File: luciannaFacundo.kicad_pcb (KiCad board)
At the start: 4 copper layers, 47 x 71.8 mm, 88 parts, among them J201 USB_B_Micro, J202 LiPo, J401 Conn_01x20, J402 Conn_01x20, Q201 MBT3904DW1, Q203 2.5A/30V, SW201 SW_DIP_x01, SW202 SW_DIP_x01, U201 MCP73831, U202 FT231XS, U203 AP2112K-3.3, U301 PCA9306, U302 ICM-20948, U401 ESP32, U402 W25Q32JVSS, Y401 26MHz, Y402 32.768kHz

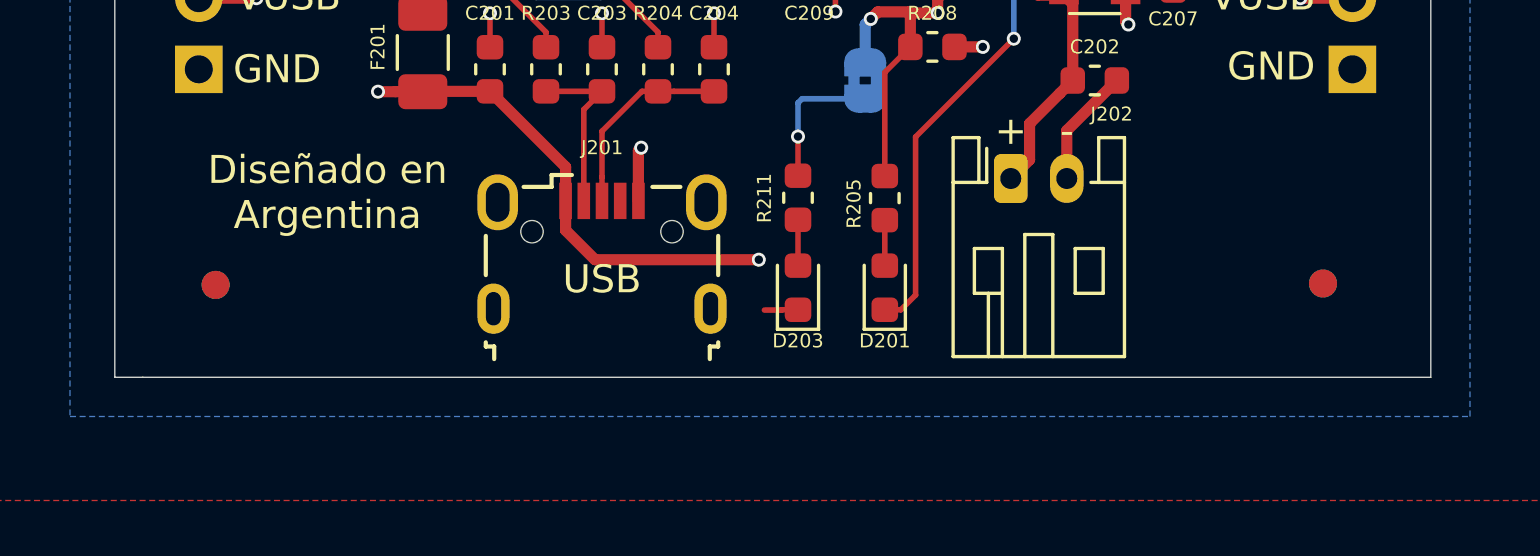
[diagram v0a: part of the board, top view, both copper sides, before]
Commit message: PMD03 - Creacion PCB y modelo 3D
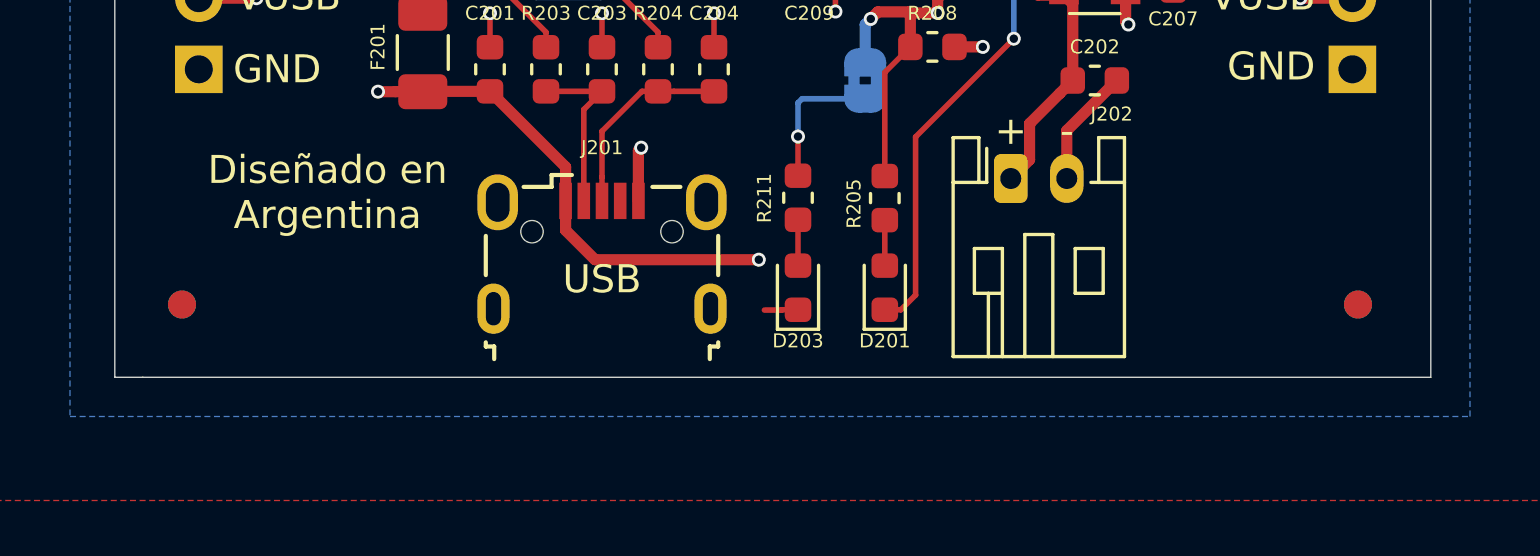
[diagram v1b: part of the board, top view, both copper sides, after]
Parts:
- moved REF03 1.46 mm to (142.0, 131.0)
- moved REF04 1.46 mm to (142.0, 131.0)
- moved REF02 1.39 mm to (100.0, 131.0)
- moved REF06 1.39 mm to (100.0, 131.0)
- moved REF** 1.34 mm to (106.0, 66.0)
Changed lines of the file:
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@@
   )
   (setup
-    (last_trace_width 0.2)
+    (last_trace_width 0.25)
     (user_trace_width 0.2)
     (user_trace_width 0.4)
@@
   )
   (module Fiducial:Fiducial_1mm_Mask3mm (layer B.Cu)
-    (at 101.2 130.3)
+    (at 100 131)
     (descr "Circular Fiducial, 1mm bare copper, 3mm soldermask opening (recommended)")
     (tags fiducial)
@@
   )
   (module Fiducial:Fiducial_1mm_Mask3mm (layer B.Cu)
-    (at 140.75 130.25)
+    (at 142 131)
     (descr "Circular Fiducial, 1mm bare copper, 3mm soldermask opening (recommended)")
     (tags fiducial)
@@
   )
   (module Fiducial:Fiducial_1mm_Mask3mm (layer F.Cu)
-    (at 140.75 130.25)
+    (at 142 131)
     (descr "Circular Fiducial, 1mm bare copper, 3mm soldermask opening (recommended)")
     (tags fiducial)
@@
   )
   (module Fiducial:Fiducial_1mm_Mask3mm (layer F.Cu)
-    (at 101.2 130.3)
+    (at 100 131)
     (descr "Circular Fiducial, 1mm bare copper, 3mm soldermask opening (recommended)")
     (tags fiducial)
@@
   )
   (module Symbol:OSHW-Symbol_6.7x6mm_SilkScreen (layer B.Cu)
-    (at 104.8 65.4 180)
+    (at 106 66 180)
     (descr "Open Source Hardware Symbol")
     (tags "Logo Symbol OSHW")
@@
     (effects (font (size 1 1) (thickness 0.15)))
   )
-  (via (at 115.6 107.8) (size 0.5) (drill 0.3) (layers F.Cu B.Cu) (net 10))
+  (segment (start 122.5875 74.45) (end 122.5875 72.9875) (width 0.75) (layer F.Cu) (net 1))
+  (segment (start 121.9 72.3) (end 121.9 71.3) (width 0.75) (layer F.Cu) (net 1))
+  (segment (start 122.5875 72.9875) (end 121.9 72.3) (width 0.75) (layer F.Cu) (net 1))
+  (segment (start 122.5875 75.45) (end 123.3 76.1625) (width 0.75) (layer F.Cu) (net 1))
+  (segment (start 122.5875 74.45) (end 122.5875 75.45) (width 0.75) (layer F.Cu) (net 1))
   (via (at 122.8 90.8) (size 0.5) (drill 0.3) (layers F.Cu B.Cu) (net 2))
   (via (at 121.2 90.8) (size 0.5) (drill 0.3) (layers F.Cu B.Cu) (net 2))
@@
   (via (at 121.2 88) (size 0.5) (drill 0.3) (layers F.Cu B.Cu) (net 2))
   (via (at 119.6 88) (size 0.5) (drill 0.3) (layers F.Cu B.Cu) (net 2))
-  (segment (start 122.5875 74.45) (end 122.5875 72.9875) (width 0.75) (layer F.Cu) (net 1))
-  (segment (start 121.9 72.3) (end 121.9 71.3) (width 0.75) (layer F.Cu) (net 1))
-  (segment (start 122.5875 72.9875) (end 121.9 72.3) (width 0.75) (layer F.Cu) (net 1))
-  (segment (start 122.5875 75.45) (end 123.3 76.1625) (width 0.75) (layer F.Cu) (net 1))
-  (segment (start 122.5875 74.45) (end 122.5875 75.45) (width 0.75) (layer F.Cu) (net 1))
   (segment (start 109.4 70.4) (end 109.625 70.625) (width 0.75) (layer In1.Cu) (net 2))
   (segment (start 130.4 79.55) (end 130.4 78.2) (width 0.2) (layer F.Cu) (net 2))
@@
   (segment (start 109.5875 98.2) (end 109.5875 99.7125) (width 0.2) (layer F.Cu) (net 9))
   (segment (start 109.45 99.85) (end 109.95 99.85) (width 0.2) (layer F.Cu) (net 9))
+  (via (at 115.6 107.8) (size 0.5) (drill 0.3) (layers F.Cu B.Cu) (net 10))
   (segment (start 118.8 97.9) (end 118.8 96.2) (width 0.2) (layer B.Cu) (net 10))
   (segment (start 118.8 96.2) (end 118.8 96.2) (width 0.2) (layer B.Cu) (net 10))

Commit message: Correcciones
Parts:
- removed REF** (x4): Fiducial_0.5mm_Mask1mm, Fiducial:Fiducial_0.5mm_Mask1mm
- removed REF**: OSHW-Symbol_6.7x6mm_SilkScreen, Symbol:OSHW-Symbol_6.7x6mm_SilkScreen
- removed REF**: KiCad-Logo2_5mm_SilkScreen, Symbol:KiCad-Logo2_5mm_SilkScreen
- removed REF01: Fiducial_1mm_Mask3m, Fiducial:Fiducial_1mm_Mask3mm
- removed REF02, REF03, REF04, REF05, REF06: Fiducial_1mm_Mask3mm, Fiducial:Fiducial_1mm_Mask3mm
- added FID101: Fiducial, Fiducial:Fiducial_1mm_Mask3mm, F.Cu at (142.0, 131.0)
- added FID102: Fiducial, Fiducial:Fiducial_1mm_Mask3mm, B.Cu at (100.0, 131.0)
- added FID103: Fiducial, Fiducial:Fiducial_1mm_Mask3mm, F.Cu at (100.0, 64.0)
- added FID104: Fiducial, Fiducial:Fiducial_1mm_Mask3mm, B.Cu at (142.0, 131.0)
- added FID105: Fiducial, Fiducial:Fiducial_1mm_Mask3mm, F.Cu at (100.0, 131.0)
- added FID106: Fiducial, Fiducial:Fiducial_1mm_Mask3mm, B.Cu at (100.0, 64.0)
- added LOGO101: Logo_Open_Hardware, Symbol:OSHW-Logo2_7.3x6mm_SilkScreen, B.Cu at (106.0, 66.0)
- added LOGO102: Logo_Kicad, Symbol:KiCad-Logo2_5mm_SilkScreen, B.Cu at (135.8, 66.0)
- J201: footprint Connector_USB:USB_Micro-B_Wuerth_629105150521 -> Connector_USB:USB_Micro-B_GCT_USB3076-30-A
- Y401: footprint Crystal:Crystal_SMD_5032-4Pin_5.0x3.2mm -> Crystal:Crystal_SMD_5032-2Pin_5.0x3.2mm
- moved C406 3.44 mm to (128.8, 92.6)
- moved C404 3.41 mm to (128.8, 86.2), turned to 0 degrees
- moved C416 0.80 mm to (108.0, 83.4)
- moved C417 0.80 mm to (108.0, 89.4)
- turned R205 to 90 degrees
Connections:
- net /Microcontrolador/CHIP_PU renamed CHIP_PU
- net /Microcontrolador/ESP32_RXD renamed ESP32_RXD
- net /Microcontrolador/ESP32_TXD renamed ESP32_TXD
- net /Microcontrolador/GPIO0 renamed GPIO0
- net /Microcontrolador/GPIO21 renamed GPIO21
- net /Microcontrolador/GPIO22 renamed GPIO22
- net /Microcontrolador/VDD1.8 renamed VDD1.8
- net /Microcontrolador/VUSB_RAW renamed VUSB_RAW
- J201 pad 6: Net-(J201-Pad6) -> GND
- R205 pad 1: VBUS -> Net-(D201-Pad2)
- R205 pad 2: Net-(D201-Pad2) -> VBUS
- Y401 pad 2: GND -> Net-(C406-Pad1)
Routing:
- net GND: track 134.8 -> 150.2 mm, vias 190 -> 189
- net Net-(C406-Pad1): track 16.2 -> 19.4 mm
- net VUSB_RAW: track 53.4 -> 55.4 mm
- net 32K_XP: track 22.4 -> 21.5 mm
- net Net-(C404-Pad2): track 9.91 -> 10.7 mm
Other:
- board text added: "3"
- board text added: "4]"
- board text added: "GPIO 0"
- board text added: "Replica ESP32 Thing. Version. 1.1 06/19"
- board text added: "Terminacion elegida: Plata por inmersión Máscara Antisoldante Fotoimageable en varias versiones Verde, Azul, Amarillo y Rojo. Impresión de serigrafia colores: Negra (para versiones antisoldantes verde y amarillo) Blanca (para versiones antisoldante rojo y azul)"
- board text added: "["
- board text added: "[1"
- board text added: "]"
- board text removed: "Replica ESP32 Thing. Version. 1.0 06/19"
